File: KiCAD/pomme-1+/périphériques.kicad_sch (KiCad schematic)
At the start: 20 parts, among them J3 ~{IRQ}, J4 rs232-socket, J5 rs232-plug, J6 5V MCU UART, J7 DE9_female, Q1 2N3904, U10 MAX232CPE

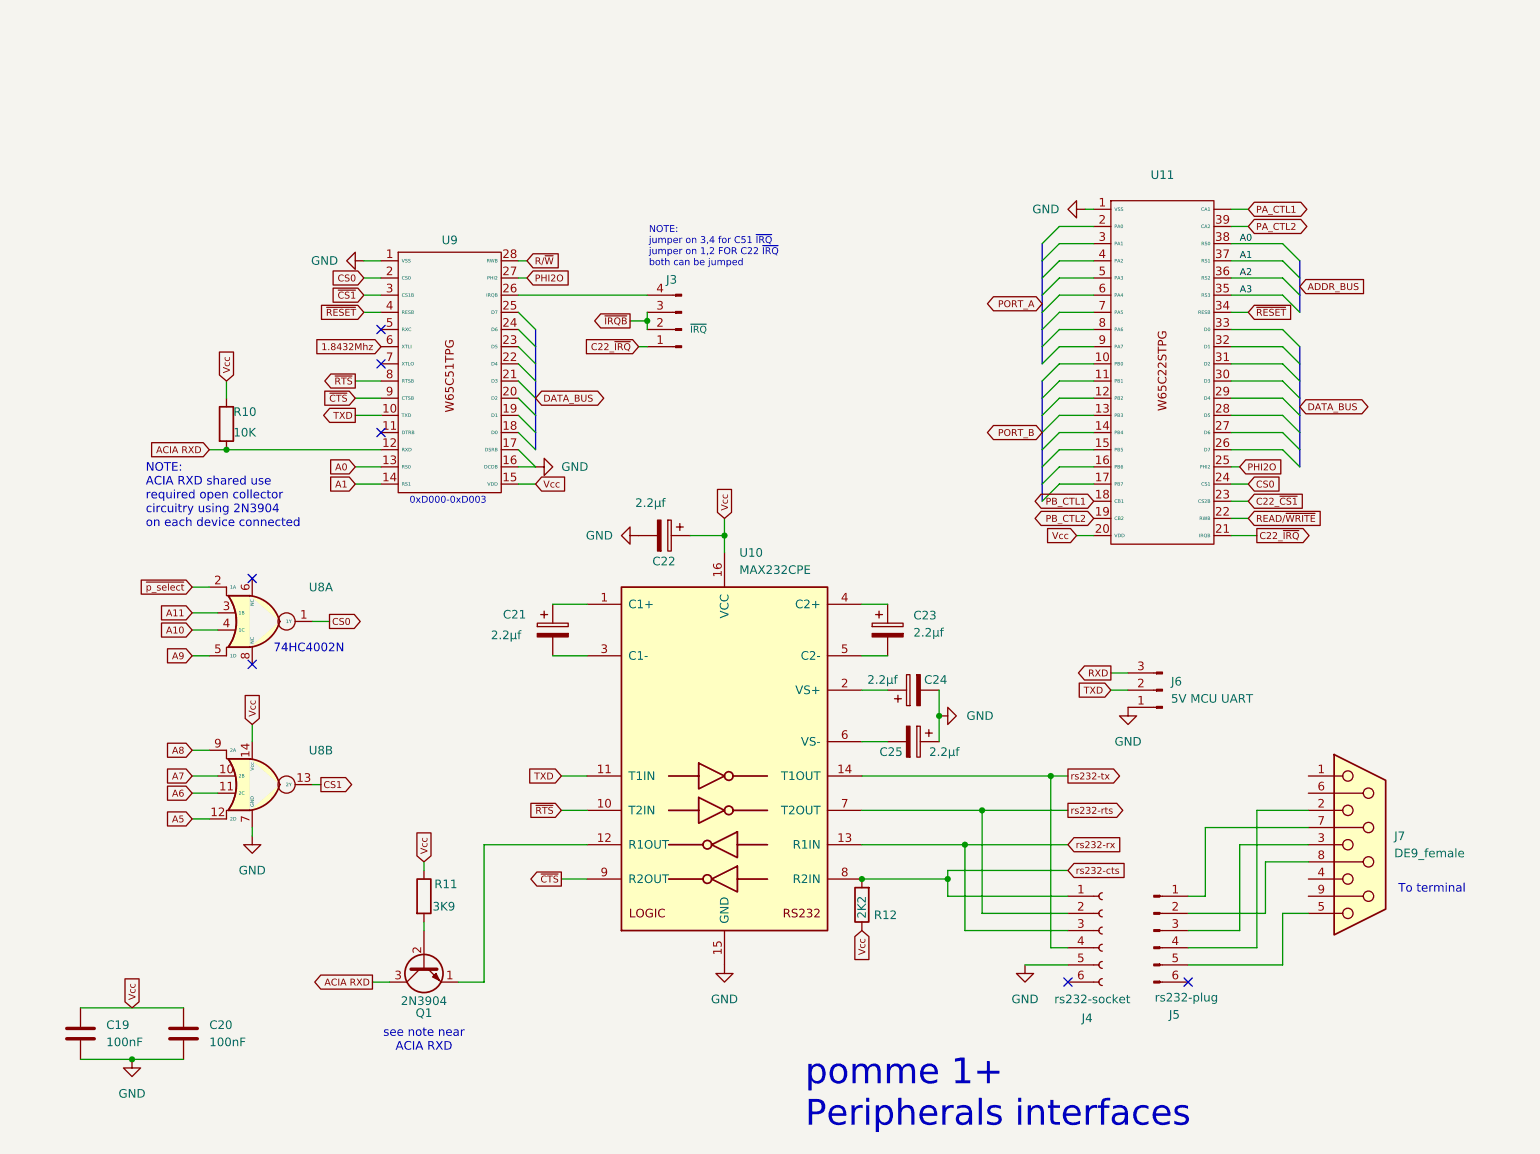
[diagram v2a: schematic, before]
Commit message: Modification schématique peripherals board
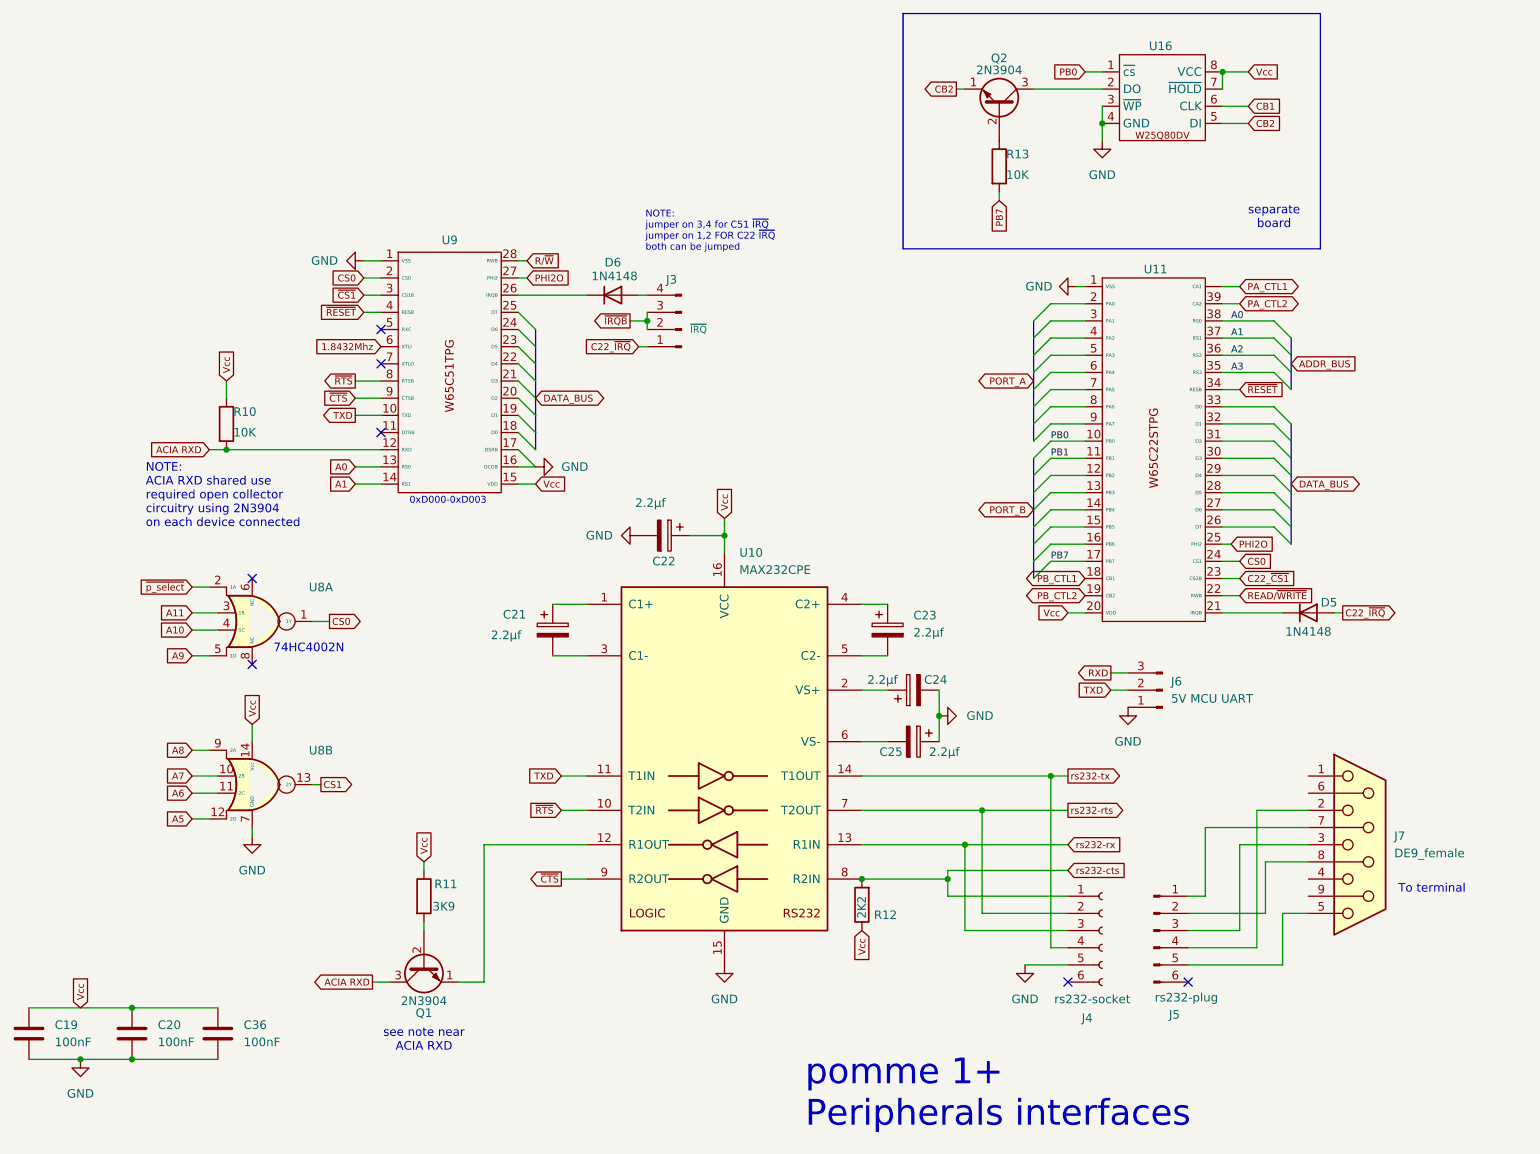
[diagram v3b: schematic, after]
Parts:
- added C36: 100nF, symbol Device:C
- added D5, D6: 1N4148, Diode_THT:D_DO-35_SOD27_P7.62mm_Horizontal, symbol Diode:1N4148
- added Q2: 2N3904, Package_TO_SOT_THT:TO-92_Inline, symbol Transistor_BJT:2N3904
- added R13: 10K, symbol Device:R
- added U16: ~, symbol W25Q80DV:W25Q80DV
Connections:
- net C22_~{IRQ}: now also D5.2 (A); no longer U11.21 (IRQB)
- net GND: now also C36.2, U16.3 (~{WP}), U16.4 (GND)
- net Vcc: now also C36.1, U16.7 (~{HOLD}), U16.8 (VCC)
- net at J3.4 (Pin_4): now also D6.2 (A); no longer U9.26 (IRQB)
- net PB0: now reaches U11.10 (PB0)
- net PB0: now also U16.1 (~{cs})
- net PB1: now reaches U11.11 (PB1)
- net PB7: now reaches U11.17 (PB7)
- net PB7: now also R13.2
- new net: Q2.2 (B), R13.1
- new net: D5.1 (K), U11.21 (IRQB)
- new net: Q2.3 (C), U16.2 (DO)
- new net: D6.1 (K), U9.26 (IRQB)
- new net CB1: U16.6 (CLK)
- new net CB2: Q2.1 (E), U16.5 (DI)
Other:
- note added: "separate board"
- moved on the sheet: C19, C20, U11

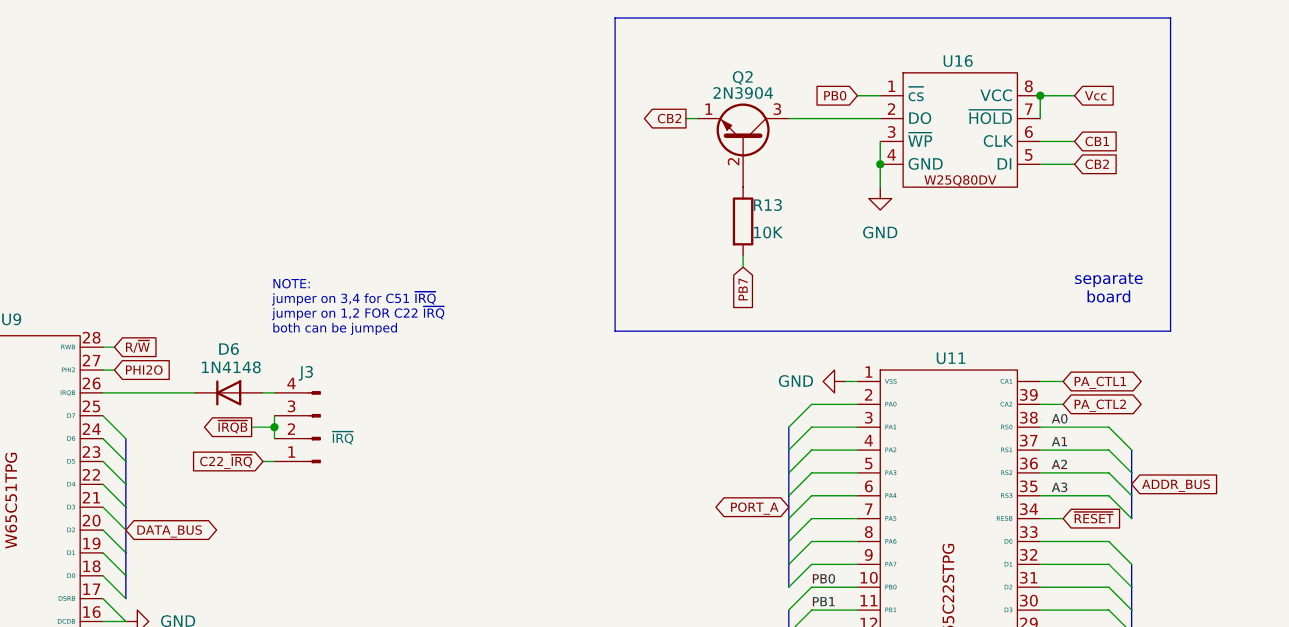
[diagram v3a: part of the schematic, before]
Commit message: Création d'une carte avec mémoire flash W25Q080DV de 1MO pour le stockage des fichiers du pomme 1+
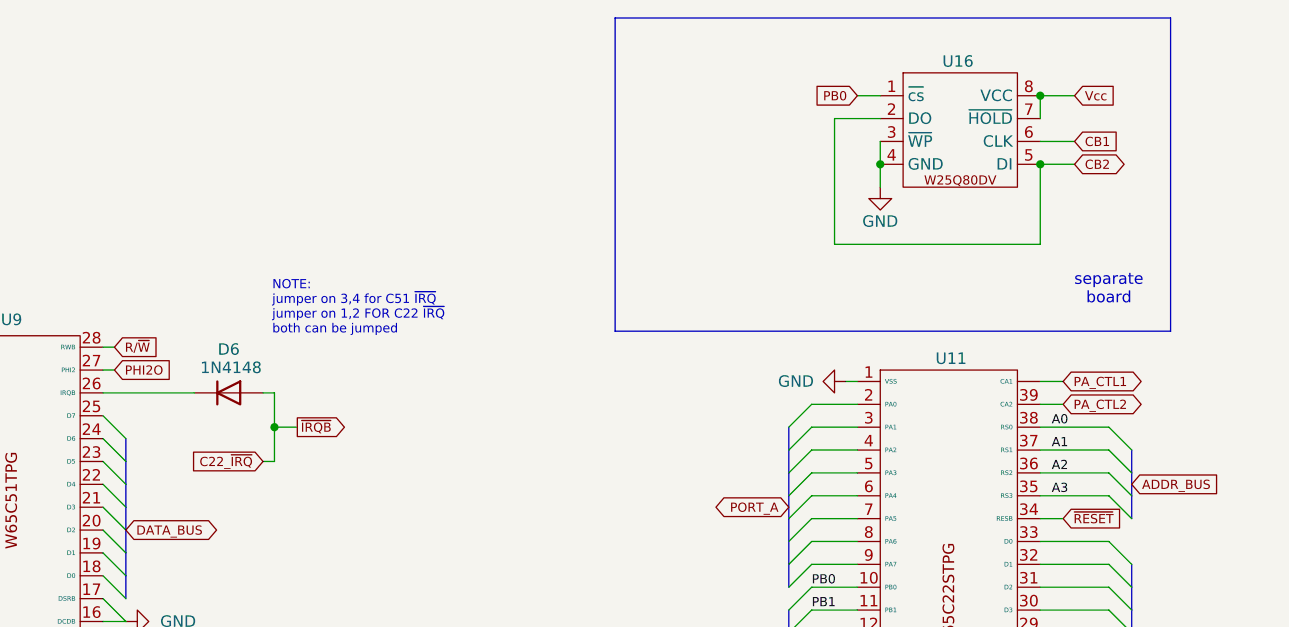
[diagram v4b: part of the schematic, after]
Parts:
- removed J3: ~{IRQ}, symbol Connector:Conn_01x04_Pin
- removed Q2: 2N3904, Package_TO_SOT_THT:TO-92_Inline, symbol Transistor_BJT:2N3904
- removed R13: 10K, symbol Device:R
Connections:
- net C22_~{IRQ}: now also D6.2 (A)
- net CB2: now also U16.2 (DO)

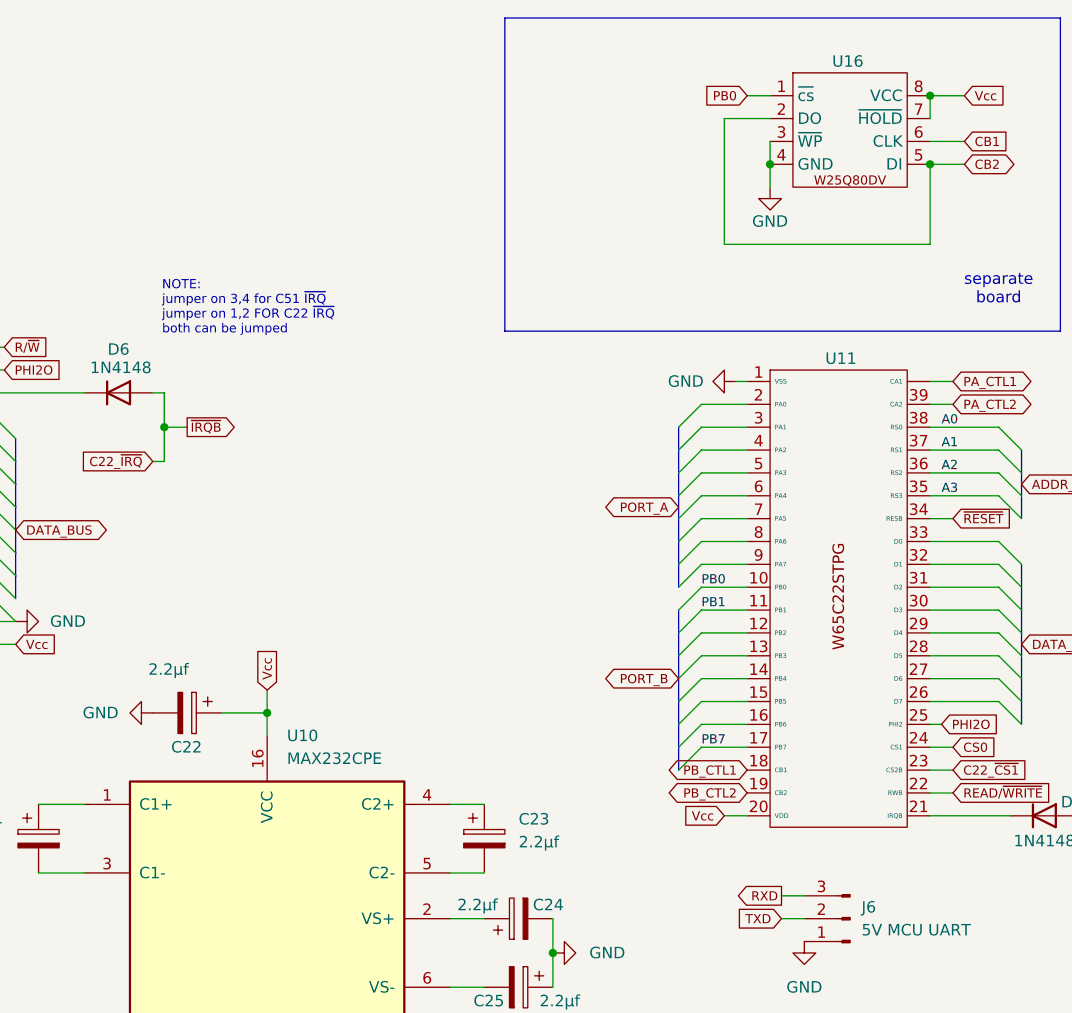
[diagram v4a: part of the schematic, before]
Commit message: Corrigé erreur dans schématique du circuit de la mémoire FLASH W25Q080DV.
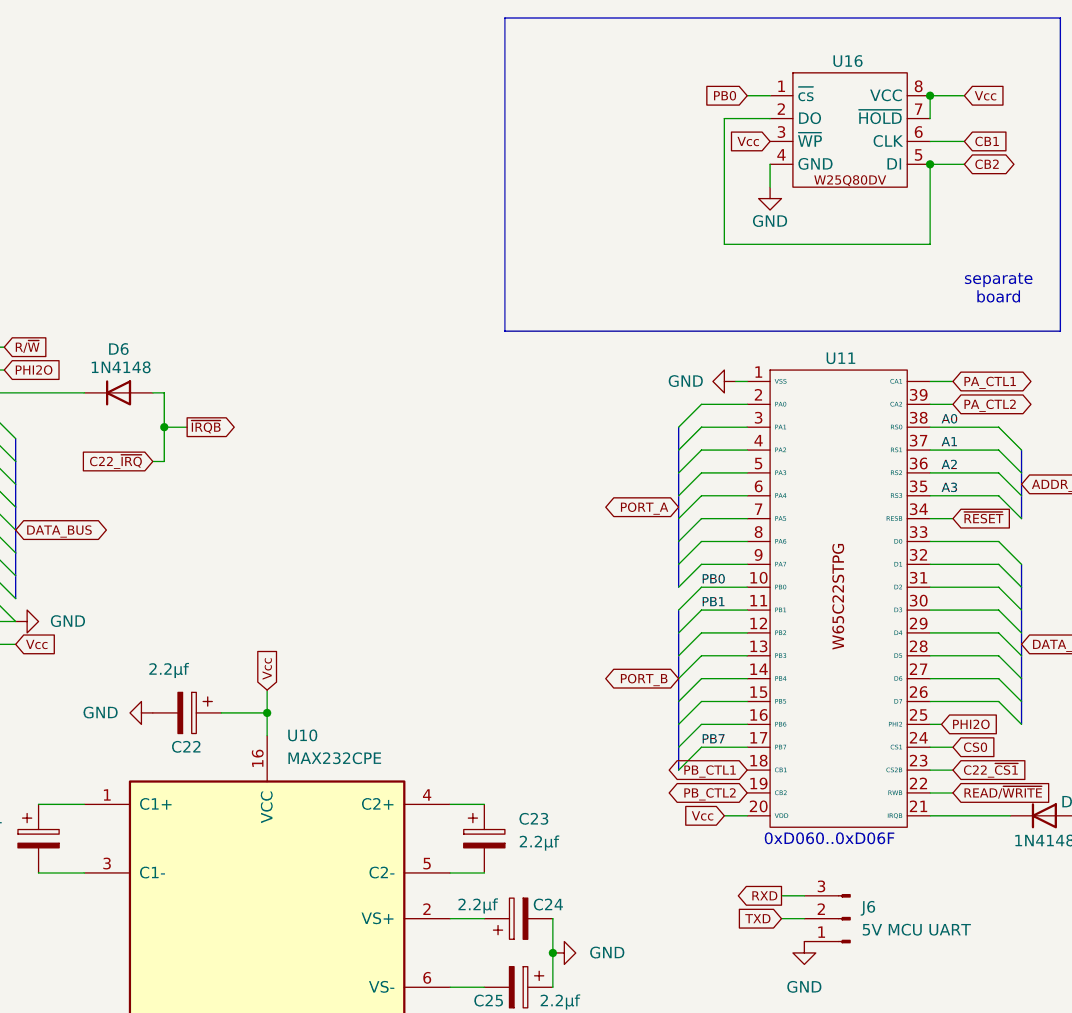
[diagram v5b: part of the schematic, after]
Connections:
- net GND: no longer U16.3 (~{WP})
- net Vcc: now also U16.3 (~{WP})
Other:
- note added: "0xD060..0xD06F"
- note removed: "NOTE: jumper on 3,4 for C51 ~{IRQ} jumper on 1,2 FOR C22 ~{IRQ} both can be jumped"
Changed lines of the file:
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@@
-	)
-	(junction
-		(at 222.25 30.48)
-		(diameter 0)
-		(color 0 0 0 0)
 	)
 	(junction
@@
 	(wire
 		(pts
-			(xy 222.25 27.94) (xy 222.25 30.48)
-		)
-		(stroke
-			(width 0)
-			(type default)
-		)
-	)
-	(wire
-		(pts
 			(xy 240.03 67.31) (xy 247.65 67.31)
 		)
@@
 		)
 	)
+	(text "0xD060..0xD06F\n"
+		(exclude_from_sim no)
+		(at 228.854 105.664 0)
+		(effects
+			(font
+				(size 1.27 1.27)
+			)
+		)
+	)
 	(text "To terminal"
 		(exclude_from_sim no)
@@
 				(size 1.27 1.27)
 			)
-		)
-	)
-	(text "NOTE:\njumper on 3,4 for C51 ~{IRQ}\njumper on 1,2 FOR C22 ~{IRQ}\nboth can be jumped"
-		(exclude_from_sim no)
-		(at 154.686 46.482 0)
-		(effects
-			(font
-				(size 1.016 1.016)
-			)
-			(justify left)
 		)
 	)
@@
 			(effects
 				(font
+					(size 1.27 1.27)
+				)
+				(justify right)
+				(hide yes)
+			)
+		)
+	)
+	(global_label "Vcc"
+		(shape input)
+		(at 222.25 27.94 180)
+		(fields_autoplaced yes)
+		(effects
+			(font
+				(size 1.016 1.016)
+			)
+			(justify right)
+		)
+		(property "Intersheetrefs" "${INTERSHEET_REFS}"
+			(at 217.2494 27.94 0)
+			(effects
+				(font
